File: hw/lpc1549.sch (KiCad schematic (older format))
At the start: 23 parts, among them J1001 ARM_JTAG_SWD_HEADER_10_PINSMD, U1001 MCP2551_SOIC8, U1002 LPC1549JBD64, X1001 XTAL_7A-12.000MAAJ-T

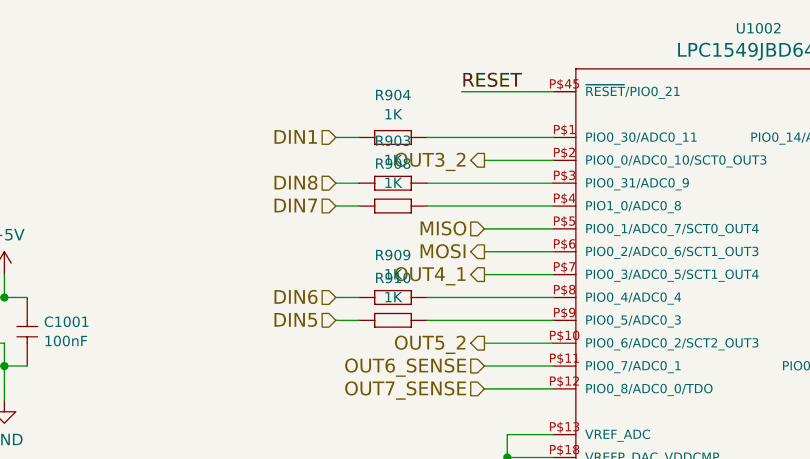
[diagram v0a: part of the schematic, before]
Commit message: 2 din replaced with ain, zeners added to outputs
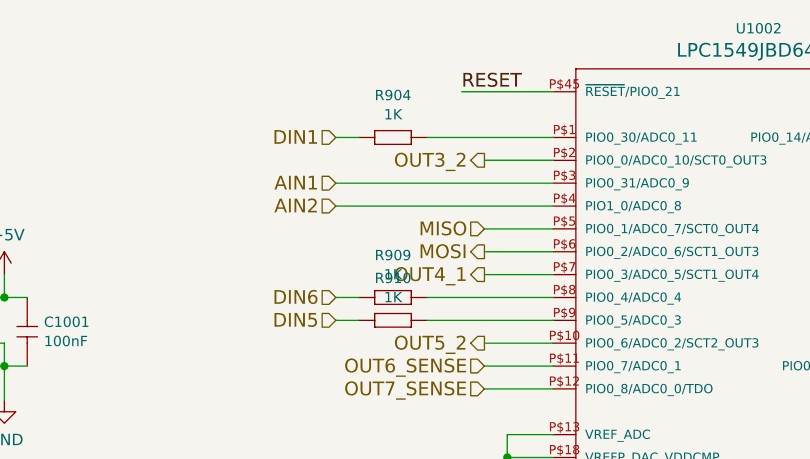
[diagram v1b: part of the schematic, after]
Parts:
- removed R903, R908: 1K, yageo:0603, symbol icu-rescue:1K
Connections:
- net AIN1: now reaches U1002.P$3 (PIO0_31/ADC0_9)
- net AIN2: now reaches U1002.P$4 (PIO1_0/ADC0_8)
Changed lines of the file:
@@
 $Descr A4 11693 8268
 encoding utf-8
-Sheet 9 11
+Sheet 9 13
 Title ""
 Date ""
@@
 DIN6
 Wire Wire Line
-	5200 2450 4650 2450
+	5200 2450 4250 2450
 Text HLabel 4250 2450 0    60   Input ~ 0
-DIN7
-Wire Wire Line
-	5200 2350 4650 2350
+AIN2
+Wire Wire Line
+	5200 2350 4250 2350
 Text HLabel 4250 2350 0    60   Input ~ 0
-DIN8
+AIN1
 Text HLabel 8300 4750 2    60   Input ~ 0
 DIN4
@@
 	3600 4100 3950 4100
 $Comp
-L icu-rescue:1K R903
-U 1 1 5B1F4296
-P 4450 2350
-F 0 "R903" H 4500 2534 45  0000 C CNN
-F 1 "1K" H 4500 2450 45  0000 C CNN
-F 2 "yageo:0603" H 4480 2500 20  0001 C CNN
-F 3 "" H 4419 2389 60  0001 C CNN
-F 4 "" H 4819 2789 60  0001 C CNN "1st Source Part Number"
-F 5 "Digikey" H 4719 2689 60  0001 C CNN "1st Source"
-F 6 "RC0603FR-071KL" H 4619 2589 60  0001 C CNN "Manufacturer Part Number"
-F 7 "YAGEO" H 4519 2489 60  0001 C CNN "Manufacturer"
-	1    4450 2350
-	1    0    0    -1
-$EndComp
-$Comp
-L icu-rescue:1K R908
-U 1 1 5B1F42DA
-P 4450 2450
-F 0 "R908" H 4500 2634 45  0000 C CNN
-F 1 "1K" H 4500 2550 45  0000 C CNN
-F 2 "yageo:0603" H 4480 2600 20  0001 C CNN
-F 3 "" H 4419 2489 60  0001 C CNN
-F 4 "" H 4819 2889 60  0001 C CNN "1st Source Part Number"
-F 5 "Digikey" H 4719 2789 60  0001 C CNN "1st Source"
-F 6 "RC0603FR-071KL" H 4619 2689 60  0001 C CNN "Manufacturer Part Number"
-F 7 "YAGEO" H 4519 2589 60  0001 C CNN "Manufacturer"
-	1    4450 2450
-	1    0    0    -1
-$EndComp
-$Comp
 L icu-rescue:1K R909
 U 1 1 5B1F431C
@@
 	4250 2850 4350 2850
 Wire Wire Line
-	4350 2450 4250 2450
-Wire Wire Line
-	4350 2350 4250 2350
-Wire Wire Line
 	5200 2650 4900 2650

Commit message: CM_6.2.1 delivered, first customer machine with CCU, HCU & ICU
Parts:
- removed R909, R910: 1K, yageo:0603, symbol icu-rescue:1K
- C1001, C1002, C1003, C1004, C1005, C1006, C1007: symbol icu-rescue:100nF -> 100nF
- C1008, C1009: symbol icu-rescue:18pF -> 18pF
- J1001: symbol icu-rescue:ARM_JTAG_SWD_HEADER_10_PINSMD -> ARM_JTAG_SWD_HEADER_10_PINSMD
- R1001, R1002: symbol icu-rescue:10K -> 10K
- R904, R905, R906, R907: symbol icu-rescue:1K -> 1K
- U1001: symbol icu-rescue:MCP2551_SOIC8 -> MCP2551_SOIC8
- U1002: symbol icu-rescue:LPC1549JBD64 -> LPC1549JBD64
- X1001: symbol icu-rescue:XTAL_7A-12.000MAAJ-T -> XTAL_7A-12.000MAAJ-T
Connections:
- net CS is gone; now on net OUT7_2: U1002.P$16 (PIO0_9/ADC1_1/TDI)
- net MISO is gone; now on net OUT3_1: U1002.P$5 (PIO0_1/ADC0_7/SCT0_OUT4)
- net MOSI is gone; now on net OUT4_2: U1002.P$6 (PIO0_2/ADC0_6/SCT1_OUT3)
- net AIN1: now also U1002.P$9 (PIO0_5/ADC0_3); no longer U1002.P$3 (PIO0_31/ADC0_9)
- net AIN2: now also U1002.P$8 (PIO0_4/ADC0_4); no longer U1002.P$4 (PIO1_0/ADC0_8)
- net OUT3_1: no longer U1002.P$23 (PIO0_11/ADC1_3)
- net OUT4_2: no longer U1002.P$25 (PIO1_2/ADC1_4)
- net OUT7_2: no longer U1002.P$39 (PIO0_17/WAKEUP/!TRST)
- net SCK: no longer names the net of U1002.P$15 (PIO1_1/ADC1_0)
- new net AIN3: U1002.P$4 (PIO1_0/ADC0_8)
- new net AIN4: U1002.P$3 (PIO0_31/ADC0_9)
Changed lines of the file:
@@
-EESchema Schematic File Version 4
+EESchema Schematic File Version 2
+LIBS:kemet
+LIBS:usevolt
+LIBS:wurth_elektronik_LED
+LIBS:power
+LIBS:yageo
 LIBS:icu-cache
 EELAYER 26 0
@@
 $Descr A4 11693 8268
 encoding utf-8
-Sheet 9 13
+Sheet 9 14
 Title ""
 Date ""
@@
 $EndDescr
 $Comp
-L icu-rescue:100nF C1007
+L 100nF C1007
 U 1 1 57E685B4
 P 5000 4200
@@
 $EndComp
 $Comp
-L icu-rescue:100nF C1006
+L 100nF C1006
 U 1 1 57E68621
 P 4650 4200
@@
 $EndComp
 $Comp
-L icu-rescue:100nF C1005
+L 100nF C1005
 U 1 1 57E68672
 P 4300 4200
@@
 $EndComp
 $Comp
-L icu-rescue:100nF C1004
+L 100nF C1004
 U 1 1 57E686C7
 P 3950 4200
@@
 $EndComp
 $Comp
-L icu-rescue:100nF C1003
+L 100nF C1003
 U 1 1 57E6871C
 P 3600 4200
@@
 $EndComp
 $Comp
-L icu-rescue:+3V3 #PWR037
+L +3V3 #PWR037
 U 1 1 57E689A3
 P 3600 3950
-AR Path="/57E689A3" Ref="#PWR037"  Part="1"
-AR Path="/57E682A9/57E689A3" Ref="#PWR037"  Part="1"
 F 0 "#PWR037" H 3600 3800 50  0001 C CNN
 F 1 "+3V3" H 3615 4123 50  0000 C CNN
@@
 $EndComp
 $Comp
-L icu-rescue:GND #PWR038
+L GND #PWR038
 U 1 1 57E689C9
 P 3600 4550
@@
 $EndComp
 $Comp
-L icu-rescue:XTAL_7A-12.000MAAJ-T X1001
+L XTAL_7A-12.000MAAJ-T X1001
 U 1 1 57E6956F
 P 7250 2950
@@
 $EndComp
 $Comp
-L icu-rescue:18pF C1008
+L 18pF C1008
 U 1 1 57E695FA
 P 7550 2750
@@
 $EndComp
 $Comp
-L icu-rescue:18pF C1009
+L 18pF C1009
 U 1 1 57E69648
 P 7550 3050
@@
 $EndComp
 $Comp
-L icu-rescue:GND #PWR039
+L GND #PWR039
 U 1 1 57E697A1
 P 8000 3100
@@
 $EndComp
 $Comp
-L icu-rescue:GND #PWR040
+L GND #PWR040
 U 1 1 57E69A8B
 P 7300 3350
@@
 $EndComp
 $Comp
-L icu-rescue:GND #PWR041
+L GND #PWR041
 U 1 1 5891FBFB
 P 9700 4500
@@
 $EndComp
 $Comp
-L icu-rescue:+3V3 #PWR042
+L +3V3 #PWR042
 U 1 1 5891FCDE
 P 9750 3450
-AR Path="/5891FCDE" Ref="#PWR042"  Part="1"
-AR Path="/57E682A9/5891FCDE" Ref="#PWR042"  Part="1"
 F 0 "#PWR042" H 9750 3300 50  0001 C CNN
 F 1 "+3V3" H 9765 3623 50  0000 C CNN
@@
 RESET
 Wire Wire Line
-	5000 4400 5000 4500
-Wire Wire Line
-	5000 4500 5100 4500
+	5000 4400 5000 4900
+Wire Wire Line
+	5000 4500 5200 4500
 Wire Wire Line
 	5200 4400 5100 4400
@@
 Connection ~ 5100 4500
 Wire Wire Line
-	3250 4100 3600 4100
+	3250 4100 5200 4100
 Connection ~ 5000 4100
 Connection ~ 4650 4100
@@
 Connection ~ 3950 4100
 Wire Wire Line
-	3250 4400 3600 4400
+	3250 4400 5000 4400
 Connection ~ 3950 4400
 Connection ~ 4300 4400
@@
 Connection ~ 5000 3550
 Wire Wire Line
-	5000 3450 5000 3550
-Wire Wire Line
-	7100 3050 7250 3050
+	5000 3450 5000 4100
+Wire Wire Line
+	7100 3050 7450 3050
 Wire Wire Line
 	7100 3050 7100 2950
@@
 	7100 2850 7100 2750
 Wire Wire Line
-	7100 2750 7250 2750
+	7100 2750 7450 2750
 Connection ~ 7250 2750
 Wire Wire Line
 	7750 2750 8000 2750
 Wire Wire Line
-	8000 2750 8000 3050
+	8000 2750 8000 3100
 Wire Wire Line
 	8000 3050 7750 3050
@@
 	7600 5150 7000 5150
 Wire Wire Line
-	9150 3950 9500 3950
-Wire Wire Line
-	7000 3750 9250 3750
-Wire Wire Line
-	9700 3850 9700 4050
+	9150 3950 9850 3950
+Wire Wire Line
+	7000 3750 9850 3750
+Wire Wire Line
+	9700 3850 9700 4500
 Wire Wire Line
 	9700 4050 9850 4050
@@
 Connection ~ 9500 3950
 Wire Wire Line
-	9250 3450 9500 3450
+	9250 3450 9750 3450
 Wire Wire Line
 	9500 3500 9500 3450
@@
 Connection ~ 9750 3450
 $Comp
-L icu-rescue:+5V #PWR043
+L +5V #PWR043
 U 1 1 58C01582
 P 2800 2750
@@
 $EndComp
 $Comp
-L icu-rescue:GND #PWR044
+L GND #PWR044
 U 1 1 58C01588
 P 2800 3300
@@
 $EndComp
 $Comp
-L icu-rescue:100nF C?
+L 100nF C?
 U 1 1 58C01592
 P 2900 2950
@@
 $EndComp
 Wire Wire Line
-	2650 2850 2800 2850
+	2650 2850 2900 2850
 Wire Wire Line
 	2800 2850 2800 2750
 Wire Wire Line
-	2650 3150 2800 3150
-Wire Wire Line
-	2800 3050 2800 3150
+	2650 3150 2900 3150
+Wire Wire Line
+	2800 3050 2800 3300
 Connection ~ 2800 3150
 Connection ~ 2800 2850
@@
 	1800 2950 1950 2950
 $Comp
-L icu-rescue:100nF C1002
+L 100nF C1002
 U 1 1 58D0A5A6
 P 3250 4200
@@
 Connection ~ 5000 4400
 $Comp
-L icu-rescue:LPC1549JBD64 U1002
+L LPC1549JBD64 U1002
 U 1 1 59C4D0FB
 P 5700 2750
@@
 	9150 3650 9150 3950
 $Comp
-L icu-rescue:MCP2551_SOIC8 U1001
+L MCP2551_SOIC8 U1001
 U 1 1 5A102A85
 P 2350 2950
@@
 	2650 3050 2800 3050
 $Comp
-L icu-rescue:10K R1002
+L 10K R1002
 U 1 1 5A533409
 P 9500 3600
@@
 $EndComp
 $Comp
-L icu-rescue:10K R1001
+L 10K R1001
 U 1 1 5A533486
 P 9250 3550
@@
 $EndComp
 $Comp
-L icu-rescue:ARM_JTAG_SWD_HEADER_10_PINSMD J1001
+L ARM_JTAG_SWD_HEADER_10_PINSMD J1001
 U 1 1 5A79DD45
 P 9950 3950
@@
 OUT2_2
 Wire Wire Line
-	5200 5550 4900 5550
-Text HLabel 4900 5550 0    60   Output ~ 0
+	5200 2550 4900 2550
+Text HLabel 4900 2550 0    60   Output ~ 0
 OUT3_1
 Wire Wire Line
@@
 OUT4_1
 Wire Wire Line
-	5200 5750 4900 5750
-Text HLabel 4900 5750 0    60   Output ~ 0
+	5200 2650 4900 2650
+Text HLabel 4900 2650 0    60   Output ~ 0
 OUT4_2
 Wire Wire Line
@@
 Text HLabel 4900 5250 0    60   Output ~ 0
 OUT7_1
-Text HLabel 8000 3450 2    60   Output ~ 0
+Wire Wire Line
+	5200 5150 4900 5150
+Text HLabel 4900 5150 0    60   Output ~ 0
 OUT7_2
 Wire Wire Line
@@
 DIN3
 $Comp
-L icu-rescue:1K R904
+L 1K R904
 U 1 1 5A7DF40A
 P 4450 2150
@@
 $EndComp
 $Comp
-L icu-rescue:1K R905
+L 1K R905
 U 1 1 5A7DF46E
 P 7750 5650
@@
 $EndComp
 $Comp
-L icu-rescue:1K R906
+L 1K R906
 U 1 1 5A7DF4BB
 P 7750 5550
@@
 	7850 5550 7950 5550
 Wire Wire Line
-	5200 2950 4650 2950
-Text HLabel 4250 2950 0    60   Input ~ 0
-DIN5
-Wire Wire Line
-	5200 2850 4650 2850
-Text HLabel 4250 2850 0    60   Input ~ 0
-DIN6
-Wire Wire Line
-	5200 2450 4250 2450
-Text HLabel 4250 2450 0    60   Input ~ 0
+	5200 2950 4900 2950
+Text HLabel 4900 2950 0    60   Input ~ 0
+AIN1
+Wire Wire Line
+	5200 2850 4900 2850
+Text HLabel 4900 2850 0    60   Input ~ 0
 AIN2
 Wire Wire Line
-	5200 2350 4250 2350
-Text HLabel 4250 2350 0    60   Input ~ 0
-AIN1
+	5200 2450 4900 2450
+Text HLabel 4900 2450 0    60   Input ~ 0
+AIN3
+Wire Wire Line
+	5200 2350 4900 2350
+Text HLabel 4900 2350 0    60   Input ~ 0
+AIN4
 Text HLabel 8300 4750 2    60   Input ~ 0
 DIN4
 $Comp
-L icu-rescue:1K R907
+L 1K R907
 U 1 1 5A8C941E
 P 8050 4750
@@
 Wire Wire Line
 	8250 4750 8300 4750
-Wire Wire Line
-	5100 4500 5200 4500
-Wire Wire Line
-	5000 4100 5200 4100
-Wire Wire Line
-	4650 4100 5000 4100
-Wire Wire Line
-	4300 4100 4650 4100
-Wire Wire Line
-	3950 4100 4300 4100
-Wire Wire Line
-	3950 4400 4300 4400
-Wire Wire Line
-	4300 4400 4650 4400
-Wire Wire Line
-	4650 4400 5000 4400
-Wire Wire Line
-	5000 4500 5000 4600
-Wire Wire Line
-	5000 4600 5000 4700
-Wire Wire Line
-	5000 4700 5000 4800
-Wire Wire Line
-	5000 4800 5000 4900
-Wire Wire Line
-	5000 4000 5000 4100
-Wire Wire Line
-	5000 3900 5000 4000
-Wire Wire Line
-	5000 3800 5000 3900
-Wire Wire Line
-	5000 3700 5000 3800
-Wire Wire Line
-	5000 3550 5000 3700
-Wire Wire Line
-	7250 3050 7450 3050
-Wire Wire Line
-	7250 2750 7450 2750
-Wire Wire Line
-	8000 3050 8000 3100
-Wire Wire Line
-	9700 4050 9700 4500
-Wire Wire Line
-	9250 3750 9850 3750
-Wire Wire Line
-	9500 3950 9850 3950
-Wire Wire Line
-	9500 3450 9750 3450
-Wire Wire Line
-	2800 3150 2900 3150
-Wire Wire Line
-	2800 3150 2800 3300
-Wire Wire Line
-	2800 2850 2900 2850
-Wire Wire Line
-	3600 4400 3950 4400
-Wire Wire Line
-	3600 4100 3950 4100
-$Comp
-L icu-rescue:1K R909
-U 1 1 5B1F431C
-P 4450 2850
-F 0 "R909" H 4500 3034 45  0000 C CNN
-F 1 "1K" H 4500 2950 45  0000 C CNN
-F 2 "yageo:0603" H 4480 3000 20  0001 C CNN
-F 3 "" H 4419 2889 60  0001 C CNN
-F 4 "" H 4819 3289 60  0001 C CNN "1st Source Part Number"
-F 5 "Digikey" H 4719 3189 60  0001 C CNN "1st Source"
-F 6 "RC0603FR-071KL" H 4619 3089 60  0001 C CNN "Manufacturer Part Number"
-F 7 "YAGEO" H 4519 2989 60  0001 C CNN "Manufacturer"
-	1    4450 2850
-	1    0    0    -1
-$EndComp
-$Comp
-L icu-rescue:1K R910
-U 1 1 5B1F436C
-P 4450 2950
-F 0 "R910" H 4500 3134 45  0000 C CNN
-F 1 "1K" H 4500 3050 45  0000 C CNN
-F 2 "yageo:0603" H 4480 3100 20  0001 C CNN
-F 3 "" H 4419 2989 60  0001 C CNN
-F 4 "" H 4819 3389 60  0001 C CNN "1st Source Part Number"
-F 5 "Digikey" H 4719 3289 60  0001 C CNN "1st Source"
-F 6 "RC0603FR-071KL" H 4619 3189 60  0001 C CNN "Manufacturer Part Number"
-F 7 "YAGEO" H 4519 3089 60  0001 C CNN "Manufacturer"
-	1    4450 2950
-	1    0    0    -1
-$EndComp
-Wire Wire Line
-	4350 2950 4250 2950
-Wire Wire Line
-	4250 2850 4350 2850
-Wire Wire Line
-	5200 2650 4900 2650
-Wire Wire Line
-	4900 2550 5200 2550
-Text HLabel 4900 2650 0    60   Output ~ 0
-MOSI
-Text HLabel 4900 2550 0    60   Input ~ 0
-MISO
-Wire Wire Line
-	5200 5150 4900 5150
-Text HLabel 4900 5150 0    60   Output ~ 0
-CS
-Wire Wire Line
-	5200 5050 4950 5050
-Text HLabel 4950 5050 0    60   Output ~ 0
-SCK
-Wire Wire Line
-	7450 3450 7450 3150
-Wire Wire Line
-	7450 3150 7000 3150
-Wire Wire Line
-	7450 3450 8000 3450
 $EndSCHEMATC

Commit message: 050518: Kikepera head prototype first revision, saw not working
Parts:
- C1001, C1002, C1003, C1004, C1005, C1006, C1007: symbol 100nF -> icu-rescue:100nF
- C1008, C1009: symbol 18pF -> icu-rescue:18pF
- J1001: symbol ARM_JTAG_SWD_HEADER_10_PINSMD -> icu-rescue:ARM_JTAG_SWD_HEADER_10_PINSMD
- R1001, R1002: symbol 10K -> icu-rescue:10K
- R904, R905, R906, R907: symbol 1K -> icu-rescue:1K
- U1001: symbol MCP2551_SOIC8 -> icu-rescue:MCP2551_SOIC8
- U1002: symbol LPC1549JBD64 -> icu-rescue:LPC1549JBD64
- X1001: symbol XTAL_7A-12.000MAAJ-T -> icu-rescue:XTAL_7A-12.000MAAJ-T
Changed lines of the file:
@@
-EESchema Schematic File Version 2
-LIBS:kemet
-LIBS:usevolt
-LIBS:wurth_elektronik_LED
-LIBS:power
-LIBS:yageo
+EESchema Schematic File Version 4
 LIBS:icu-cache
 EELAYER 26 0
@@
 $EndDescr
 $Comp
-L 100nF C1007
+L icu-rescue:100nF C1007
 U 1 1 57E685B4
 P 5000 4200
@@
 $EndComp
 $Comp
-L 100nF C1006
+L icu-rescue:100nF C1006
 U 1 1 57E68621
 P 4650 4200
@@
 $EndComp
 $Comp
-L 100nF C1005
+L icu-rescue:100nF C1005
 U 1 1 57E68672
 P 4300 4200
@@
 $EndComp
 $Comp
-L 100nF C1004
+L icu-rescue:100nF C1004
 U 1 1 57E686C7
 P 3950 4200
@@
 $EndComp
 $Comp
-L 100nF C1003
+L icu-rescue:100nF C1003
 U 1 1 57E6871C
 P 3600 4200
@@
 $EndComp
 $Comp
-L +3V3 #PWR037
+L icu-rescue:+3V3 #PWR037
 U 1 1 57E689A3
 P 3600 3950
+AR Path="/57E689A3" Ref="#PWR037"  Part="1"
+AR Path="/57E682A9/57E689A3" Ref="#PWR037"  Part="1"
 F 0 "#PWR037" H 3600 3800 50  0001 C CNN
 F 1 "+3V3" H 3615 4123 50  0000 C CNN
@@
 $EndComp
 $Comp
-L GND #PWR038
+L icu-rescue:GND #PWR038
 U 1 1 57E689C9
 P 3600 4550
@@
 $EndComp
 $Comp
-L XTAL_7A-12.000MAAJ-T X1001
+L icu-rescue:XTAL_7A-12.000MAAJ-T X1001
 U 1 1 57E6956F
 P 7250 2950
@@
 $EndComp
 $Comp
-L 18pF C1008
+L icu-rescue:18pF C1008
 U 1 1 57E695FA
 P 7550 2750
@@
 $EndComp
 $Comp
-L 18pF C1009
+L icu-rescue:18pF C1009
 U 1 1 57E69648
 P 7550 3050
@@
 $EndComp
 $Comp
-L GND #PWR039
+L icu-rescue:GND #PWR039
 U 1 1 57E697A1
 P 8000 3100
@@
 $EndComp
 $Comp
-L GND #PWR040
+L icu-rescue:GND #PWR040
 U 1 1 57E69A8B
 P 7300 3350
@@
 $EndComp
 $Comp
-L GND #PWR041
+L icu-rescue:GND #PWR041
 U 1 1 5891FBFB
 P 9700 4500
@@
 $EndComp
 $Comp
-L +3V3 #PWR042
+L icu-rescue:+3V3 #PWR042
 U 1 1 5891FCDE
 P 9750 3450
+AR Path="/5891FCDE" Ref="#PWR042"  Part="1"
+AR Path="/57E682A9/5891FCDE" Ref="#PWR042"  Part="1"
 F 0 "#PWR042" H 9750 3300 50  0001 C CNN
 F 1 "+3V3" H 9765 3623 50  0000 C CNN
@@
 RESET
 Wire Wire Line
-	5000 4400 5000 4900
-Wire Wire Line
-	5000 4500 5200 4500
+	5000 4400 5000 4500
+Wire Wire Line
+	5000 4500 5100 4500
 Wire Wire Line
 	5200 4400 5100 4400
@@
 Connection ~ 5100 4500
 Wire Wire Line
-	3250 4100 5200 4100
+	3250 4100 3600 4100
 Connection ~ 5000 4100
 Connection ~ 4650 4100
@@
 Connection ~ 3950 4100
 Wire Wire Line
-	3250 4400 5000 4400
+	3250 4400 3600 4400
 Connection ~ 3950 4400
 Connection ~ 4300 4400
@@
 Connection ~ 5000 3550
 Wire Wire Line
-	5000 3450 5000 4100
-Wire Wire Line
-	7100 3050 7450 3050
+	5000 3450 5000 3550
+Wire Wire Line
+	7100 3050 7250 3050
 Wire Wire Line
 	7100 3050 7100 2950
@@
 	7100 2850 7100 2750
 Wire Wire Line
-	7100 2750 7450 2750
+	7100 2750 7250 2750
 Connection ~ 7250 2750
 Wire Wire Line
 	7750 2750 8000 2750
 Wire Wire Line
-	8000 2750 8000 3100
+	8000 2750 8000 3050
 Wire Wire Line
 	8000 3050 7750 3050
@@
 	7600 5150 7000 5150
 Wire Wire Line
-	9150 3950 9850 3950
-Wire Wire Line
-	7000 3750 9850 3750
-Wire Wire Line
-	9700 3850 9700 4500
+	9150 3950 9500 3950
+Wire Wire Line
+	7000 3750 9250 3750
+Wire Wire Line
+	9700 3850 9700 4050
 Wire Wire Line
 	9700 4050 9850 4050
@@
 Connection ~ 9500 3950
 Wire Wire Line
-	9250 3450 9750 3450
+	9250 3450 9500 3450
 Wire Wire Line
 	9500 3500 9500 3450
@@
 Connection ~ 9750 3450
 $Comp
-L +5V #PWR043
+L icu-rescue:+5V #PWR043
 U 1 1 58C01582
 P 2800 2750
@@
 $EndComp
 $Comp
-L GND #PWR044
+L icu-rescue:GND #PWR044
 U 1 1 58C01588
 P 2800 3300
@@
 $EndComp
 $Comp
-L 100nF C?
+L icu-rescue:100nF C?
 U 1 1 58C01592
 P 2900 2950
@@
 $EndComp
 Wire Wire Line
-	2650 2850 2900 2850
+	2650 2850 2800 2850
 Wire Wire Line
 	2800 2850 2800 2750
 Wire Wire Line
-	2650 3150 2900 3150
-Wire Wire Line
-	2800 3050 2800 3300
+	2650 3150 2800 3150
+Wire Wire Line
+	2800 3050 2800 3150
 Connection ~ 2800 3150
 Connection ~ 2800 2850
@@
 	1800 2950 1950 2950
 $Comp
-L 100nF C1002
+L icu-rescue:100nF C1002
 U 1 1 58D0A5A6
 P 3250 4200
@@
 Connection ~ 5000 4400
 $Comp
-L LPC1549JBD64 U1002
+L icu-rescue:LPC1549JBD64 U1002
 U 1 1 59C4D0FB
 P 5700 2750
@@
 	9150 3650 9150 3950
 $Comp
-L MCP2551_SOIC8 U1001
+L icu-rescue:MCP2551_SOIC8 U1001
 U 1 1 5A102A85
 P 2350 2950
@@
 	2650 3050 2800 3050
 $Comp
-L 10K R1002
+L icu-rescue:10K R1002
 U 1 1 5A533409
 P 9500 3600
@@
 $EndComp
 $Comp
-L 10K R1001
+L icu-rescue:10K R1001
 U 1 1 5A533486
 P 9250 3550
@@
 $EndComp
 $Comp
-L ARM_JTAG_SWD_HEADER_10_PINSMD J1001
+L icu-rescue:ARM_JTAG_SWD_HEADER_10_PINSMD J1001
 U 1 1 5A79DD45
 P 9950 3950
@@
 DIN3
 $Comp
-L 1K R904
+L icu-rescue:1K R904
 U 1 1 5A7DF40A
 P 4450 2150
@@
 $EndComp
 $Comp
-L 1K R905
+L icu-rescue:1K R905
 U 1 1 5A7DF46E
 P 7750 5650
@@
 $EndComp
 $Comp
-L 1K R906
+L icu-rescue:1K R906
 U 1 1 5A7DF4BB
 P 7750 5550
@@
 DIN4
 $Comp
-L 1K R907
+L icu-rescue:1K R907
 U 1 1 5A8C941E
 P 8050 4750
@@
 Wire Wire Line
 	8250 4750 8300 4750
+Wire Wire Line
+	5100 4500 5200 4500
+Wire Wire Line
+	5000 4100 5200 4100
+Wire Wire Line
+	4650 4100 5000 4100
+Wire Wire Line
+	4300 4100 4650 4100
+Wire Wire Line
+	3950 4100 4300 4100
+Wire Wire Line
+	3950 4400 4300 4400
+Wire Wire Line
+	4300 4400 4650 4400
+Wire Wire Line
+	4650 4400 5000 4400
+Wire Wire Line
+	5000 4500 5000 4600
+Wire Wire Line
+	5000 4600 5000 4700
+Wire Wire Line
+	5000 4700 5000 4800
+Wire Wire Line
+	5000 4800 5000 4900
+Wire Wire Line
+	5000 4000 5000 4100
+Wire Wire Line
+	5000 3900 5000 4000
+Wire Wire Line
+	5000 3800 5000 3900
+Wire Wire Line
+	5000 3700 5000 3800
+Wire Wire Line
+	5000 3550 5000 3700
+Wire Wire Line
+	7250 3050 7450 3050
+Wire Wire Line
+	7250 2750 7450 2750
+Wire Wire Line
+	8000 3050 8000 3100
+Wire Wire Line
+	9700 4050 9700 4500
+Wire Wire Line
+	9250 3750 9850 3750
+Wire Wire Line
+	9500 3950 9850 3950
+Wire Wire Line
+	9500 3450 9750 3450
+Wire Wire Line
+	2800 3150 2900 3150
+Wire Wire Line
+	2800 3150 2800 3300
+Wire Wire Line
+	2800 2850 2900 2850
+Wire Wire Line
+	3600 4400 3950 4400
+Wire Wire Line
+	3600 4100 3950 4100
 $EndSCHEMATC
